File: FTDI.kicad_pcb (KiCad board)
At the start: 2 copper layers, 20 x 26 mm, 13 parts, among them J1 USB_B_Micro, J2 Conn_01x07, U1 FT232RL-REEL

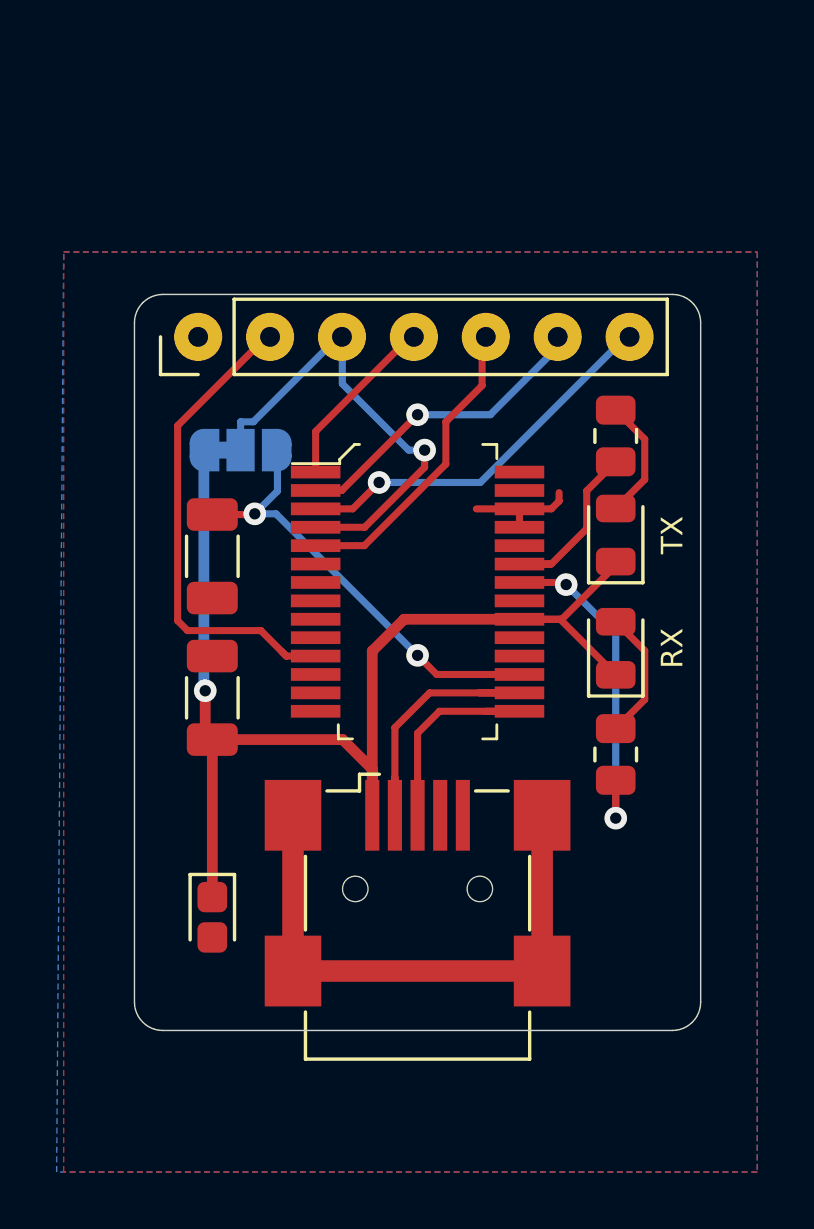
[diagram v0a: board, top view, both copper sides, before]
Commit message: V1.1 - adding 27 Ohm resistors and 47pF Capacitor for noise redutions in the D+ and D- lines
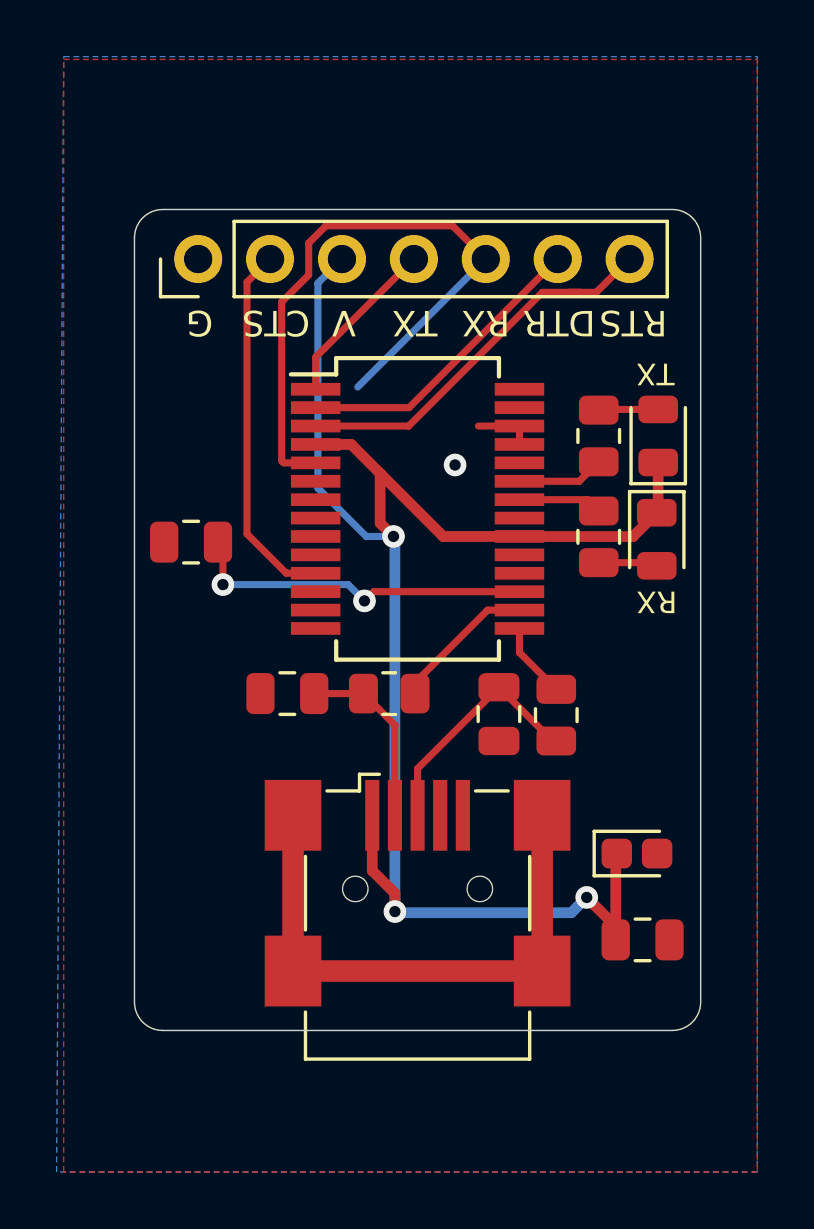
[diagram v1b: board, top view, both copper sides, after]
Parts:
- removed G***: OSHW-logo_silkscreen-back_3mm, OSHW-logo:OSHW-logo_silkscreen-back_3mm
- removed JP1: Default Output, Jumper:SolderJumper-3_P1.3mm_Bridged12_RoundedPad1.0x1.5mm
- removed REF**: fullstacklogo, jareas_custom:fullstacklogo
- added C1: 47pF, Capacitor_SMD:C_0805_2012Metric, F.Cu at (2.88, -6.17)
- added C2: 47pF, Capacitor_SMD:C_0805_2012Metric, F.Cu at (-4.60, -6.90)
- added R1: 27, Resistor_SMD:R_0805_2012Metric, F.Cu at (-1.00, -6.90)
- added R2: 27, Resistor_SMD:R_0805_2012Metric, F.Cu at (4.90, -6.14)
- C3: renamed from C1; footprint Capacitor_SMD:C_1206_3216Metric -> Capacitor_SMD:C_0805_2012Metric
- C5: renamed from C3; footprint Capacitor_SMD:C_1206_3216Metric -> Capacitor_SMD:C_0805_2012Metric
- J2: footprint jareas_custom:PinHeader_1x07_P2.54mm_H0.7mm_Vertical -> jareas_custom:PinHeader_1x07_P2.54mm_H1mm_Vertical
- U1: footprint digikey-footprints:SSOP-28_W5.30mm -> Package_SO:SSOP-28_5.3x10.2mm_P0.65mm
- moved C3 17.4 mm to (7.95, 1.80), turned to 180 degrees
- moved C4 15.2 mm to (7.75, -1.25), turned to 0 degrees
- moved R4 7.71 mm to (6.40, -12.4), turned to 90 degrees
- moved D2 4.11 mm to (8.45, -12.3), turned to 270 degrees
- moved D1 3.81 mm to (8.50, -16.0)
- moved U1 2.93 mm to (0.00, -13.4), turned to 0 degrees
- moved J2 2.75 mm to (-7.75, -22.2)
- moved C5 0.90 mm to (-8.00, -12.2), turned to 0 degrees
- moved R3 0.60 mm to (6.40, -16.0)
- renumbered C2 to C4, R1 to R3, R2 to R4
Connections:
- net +3V3 renamed Net-(C5-Pad2)
- J1 pad 2: D- -> Net-(C2-Pad2)
- J1 pad 3: D+ -> Net-(C1-Pad2)
- J2 pad 3: VOUT -> +5V
- U1 pad 4: VOUT -> +5V
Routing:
- net VOUT: track 18.6 -> 0.00 mm, vias 1 -> 0
- net +5V: track 42.7 -> 58.8 mm, vias 1 -> 3
- net RXD: track 11.8 -> 22.7 mm
- net Net-(R4-Pad2): track 12.1 -> 2.97 mm, vias 2 -> 0
- net Net-(C1-Pad2): track 0.00 -> 8.53 mm
- net D+: track 9.32 -> 2.69 mm
- net Net-(C2-Pad2): track 0.00 -> 6.50 mm
- net D-: track 10.8 -> 5.14 mm
- net CTS: track 17.7 -> 13.0 mm
- net Net-(C5-Pad2): track 16.8 -> 12.4 mm
- net Net-(R3-Pad2): track 6.71 -> 3.08 mm
- net Net-(D2-Pad2): track 4.62 -> 2.10 mm
- net Net-(D1-Pad2): track 4.32 -> 2.11 mm
- net GND: track 3.99 -> 2.10 mm, vias 0 -> 1
- net TXD: track 7.16 -> 6.04 mm
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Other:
- board size 20 x 26 mm -> 20 x 29 mm
- board text added: "Basic FTDI - 5V V1.1"
